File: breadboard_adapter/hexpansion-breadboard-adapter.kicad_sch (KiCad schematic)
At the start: 3 parts, among them J1 Conn_02x10_Counter_Clockwise, J2 Conn_01x10_Pin, J3 Conn_01x10_Pin

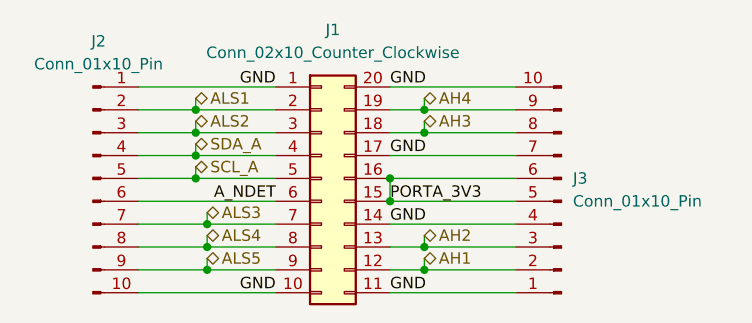
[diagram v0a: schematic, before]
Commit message: Update Breadboard Adapter.
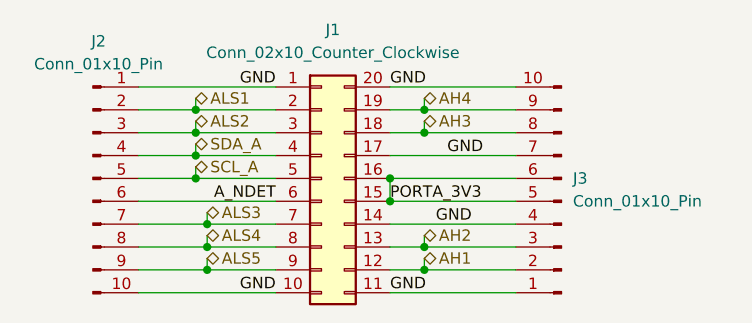
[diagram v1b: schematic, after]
